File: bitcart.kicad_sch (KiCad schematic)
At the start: 8 parts

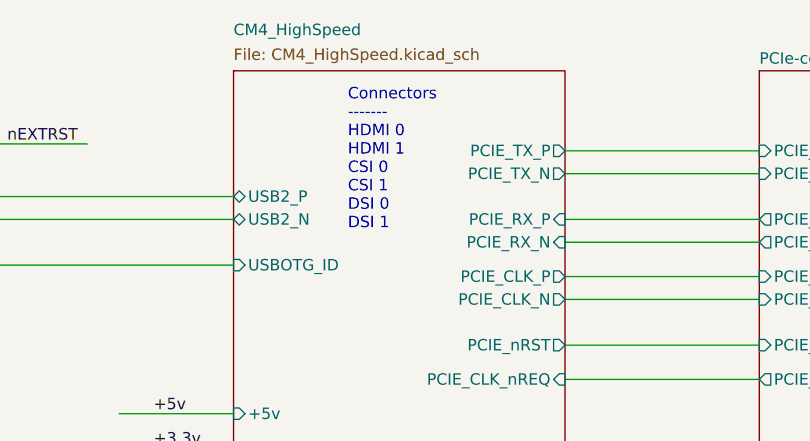
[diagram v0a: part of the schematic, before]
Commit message: removed HDMI, CAM and DISP1 connectors
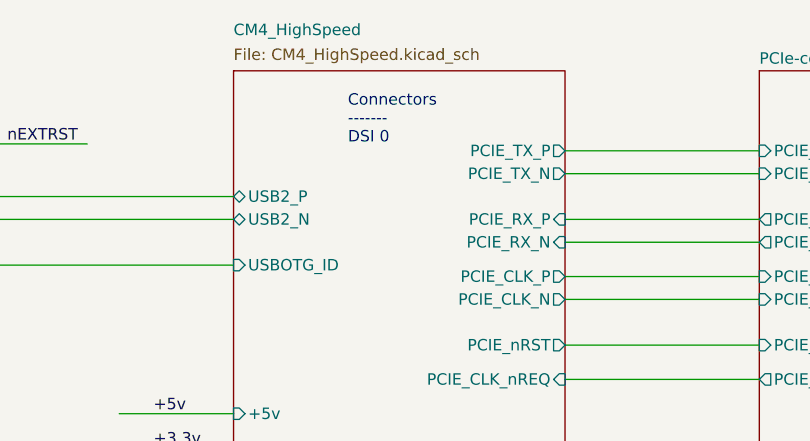
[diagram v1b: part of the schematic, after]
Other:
- note added: "Connectors ------- DSI 0"
- note removed: "Connectors ------- HDMI 0 HDMI 1 CSI 0 CSI 1 DSI 0 DSI 1"
- company: © 2020-2022 Raspberry Pi Ltd (formerly Raspberry Pi (Trading) Ltd.) -> (none)
- title: Compute Module 4 IO Board - Top Level -> Bitcart
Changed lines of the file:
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@@
   (paper "A4")
   (title_block
-    (title "Compute Module 4 IO Board - Top Level")
+    (title "Bitcart")
+    (date "2023-09-15")
     (rev "1")
-    (company "© 2020-2022 Raspberry Pi Ltd (formerly Raspberry Pi (Trading) Ltd.)")
-    (comment 1 "www.raspberrypi.com")
   )
   (junction (at 140.97 110.49) (diameter 1.016) (color 0 0 0 0)
@@
     (effects (font (size 1.27 1.27)) (justify left bottom))
   )
-  (text "Connectors\n-------\nHDMI 0\nHDMI 1\nCSI 0\nCSI 1\nDSI 0\nDSI 1"
-    (at 144.78 57.15 0)
+  (text "Connectors\n-------\nDSI 0" (at 144.78 47.625 0)
     (effects (font (size 1.27 1.27)) (justify left bottom))
   )
@@
   (sheet (at 81.28 39.878) (size 24.13 28.702)
     (stroke (width 0.1524) (type solid) (color 132 0 132 1))
-    (fill (color 255 255 255 0.0000))
+    (fill (color 255 255 194 1.0000))
     (property "Sheetname" "USB2-HUB" (at 81.28 39.2425 0)
       (effects (font (size 1.27 1.27)) (justify left bottom))

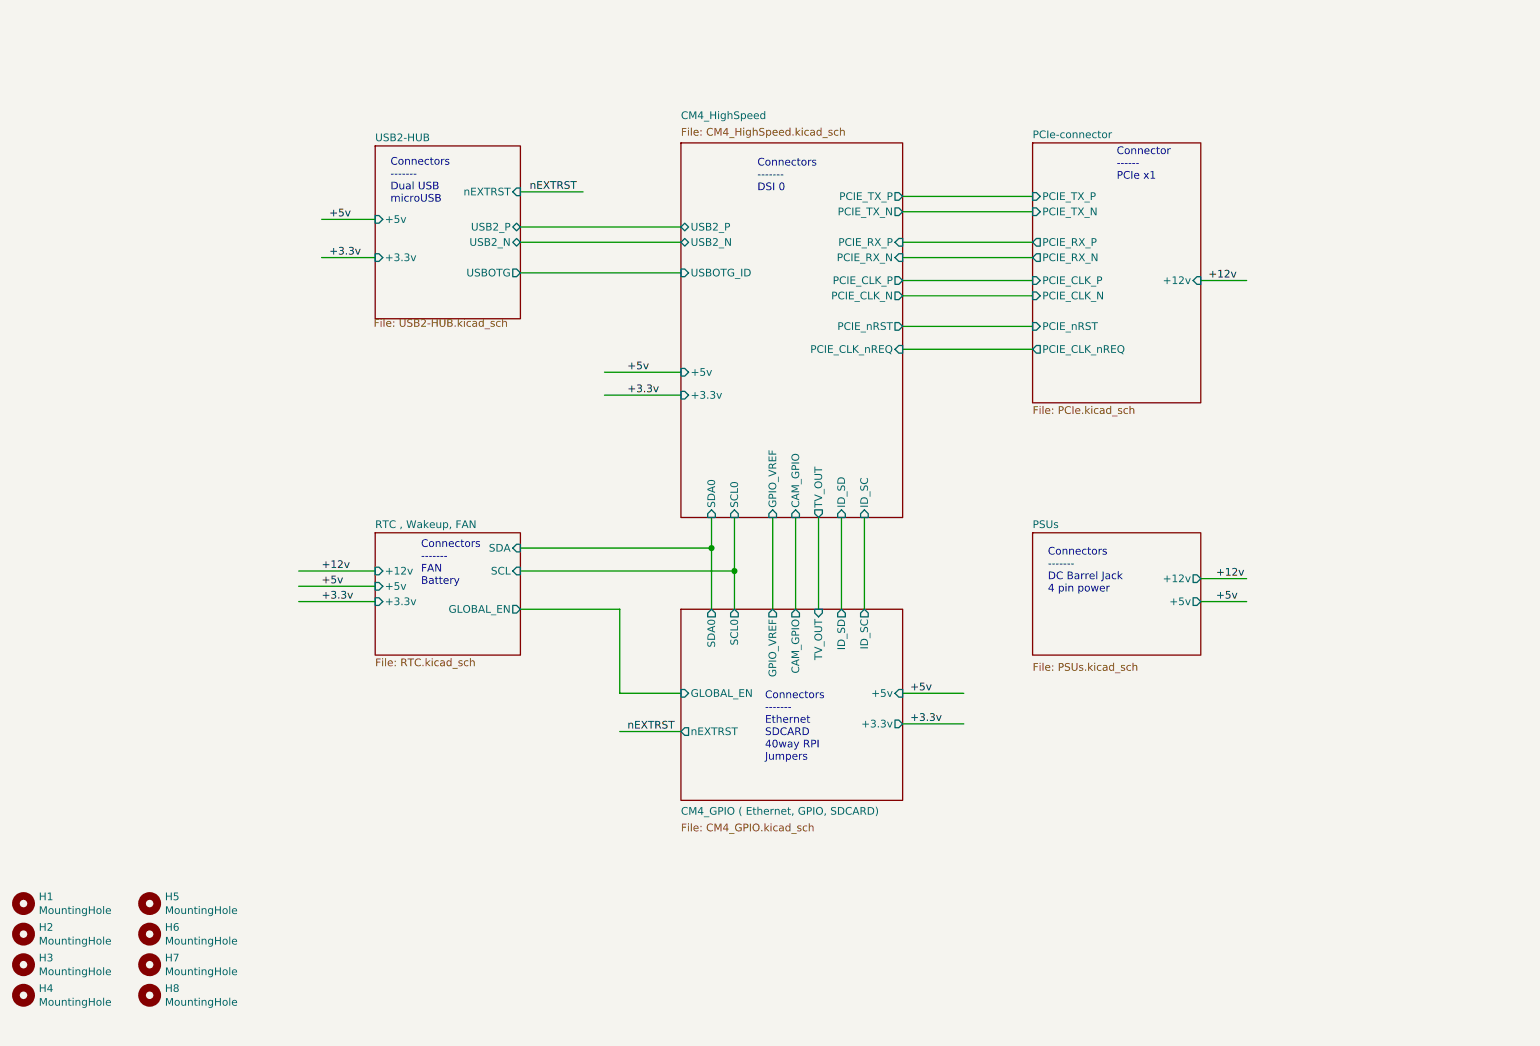
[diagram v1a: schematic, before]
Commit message: added hashboard connectors. added GPU power connector
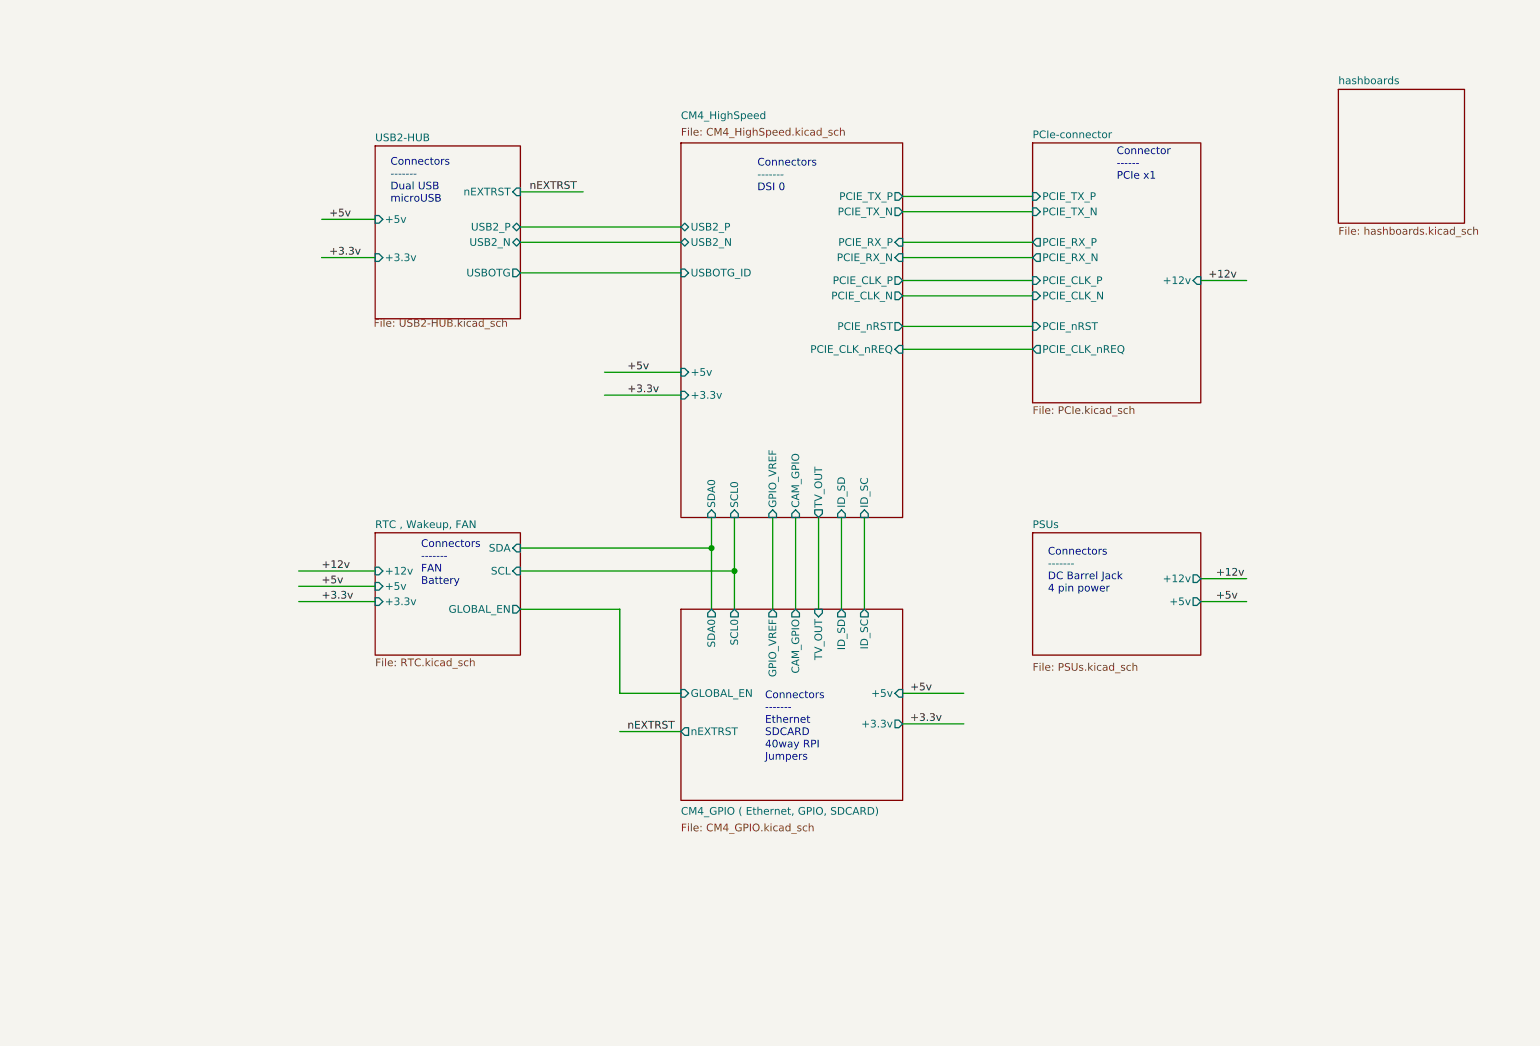
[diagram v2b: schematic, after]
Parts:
- removed H1, H2, H3, H4, H5, H6, H7, H8: MountingHole, MountingHole:MountingHole_2.7mm_M2.5, symbol Mechanical:MountingHole
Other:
- added sheet hashboards (hashboards.kicad_sch)

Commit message: extended the board to make room for IO connectors. added the vertical display connector.
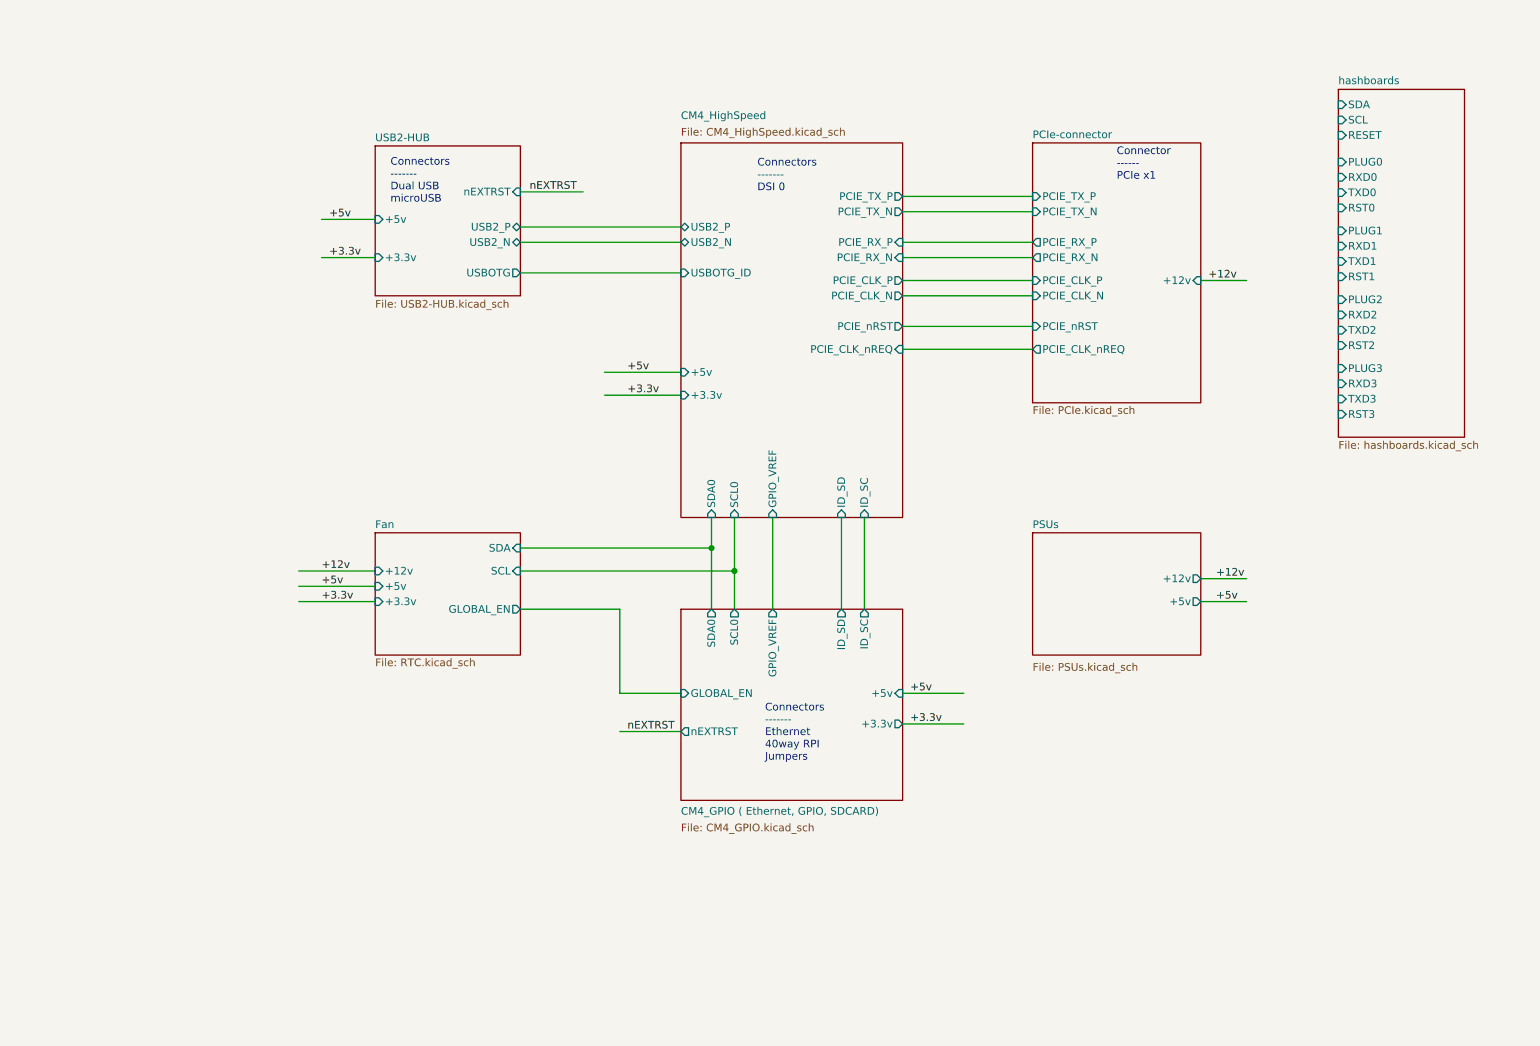
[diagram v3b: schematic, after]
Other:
- sheet RTC , Wakeup, FAN renamed Fan
- sheet CM4_GPIO ( Ethernet, GPIO, SDCARD) ports: added none; removed CAM_GPIO, TV_OUT
- sheet CM4_HighSpeed ports: added none; removed CAM_GPIO, TV_OUT
- sheet hashboards ports: added PLUG0, PLUG1, PLUG2, PLUG3, RESET, RST0, RST1, RST2, RST3, RXD0, RXD1, RXD2, RXD3, SCL, SDA, TXD0, TXD1, TXD2, TXD3; removed none
- note added: "Connectors ------- Ethernet 40way RPI Jumpers"
- note removed: "Connectors ------- DC Barrel Jack 4 pin power"
- note removed: "Connectors ------- Ethernet SDCARD 40way RPI Jumpers"
- note removed: "Connectors ------- FAN Battery"
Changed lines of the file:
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@@
-    (stroke (width 0) (type solid))
-  )
-  (wire (pts (xy 151.13 116.84) (xy 151.13 101.6))
     (stroke (width 0) (type solid))
   )
@@
     (stroke (width 0) (type solid))
   )
-  (wire (pts (xy 154.94 116.84) (xy 154.94 101.6))
-    (stroke (width 0) (type solid))
-  )
   (wire (pts (xy 105.41 60.96) (xy 132.08 60.96))
     (stroke (width 0) (type solid))
@@
     (stroke (width 0) (type solid))
   )
-  (text "Connectors\n-------\nFAN\nBattery" (at 88.9 113.03 0)
-    (effects (font (size 1.27 1.27)) (justify left bottom))
-  )
   (text "Connector\n------\nPCIe x1" (at 204.47 45.72 0)
     (effects (font (size 1.27 1.27)) (justify left bottom))
   )
-  (text "Connectors\n-------\nDC Barrel Jack\n4 pin power" (at 193.04 114.3 0)
-    (effects (font (size 1.27 1.27)) (justify left bottom))
-  )
   (text "Connectors\n-------\nDual USB\nmicroUSB" (at 83.82 49.53 0)
     (effects (font (size 1.27 1.27)) (justify left bottom))
   )
-  (text "Connectors\n-------\nEthernet\nSDCARD\n40way RPI\nJumpers"
-    (at 146.05 142.24 0)
+  (text "Connectors\n-------\nEthernet\n40way RPI\nJumpers" (at 146.05 142.24 0)
     (effects (font (size 1.27 1.27)) (justify left bottom))
   )
@@
       (effects (font (size 1.27 1.27)) (justify right))
     )
-    (pin "CAM_GPIO" output (at 151.13 116.84 90)
-      (effects (font (size 1.27 1.27)) (justify right))
-    )
     (pin "SCL0" output (at 140.97 116.84 90)
       (effects (font (size 1.27 1.27)) (justify right))
@@
       (effects (font (size 1.27 1.27)) (justify right))
     )
-    (pin "TV_OUT" input (at 154.94 116.84 90)
-      (effects (font (size 1.27 1.27)) (justify right))
-    )
     (instances
       (project "bitcart"
@@
       (effects (font (size 1.27 1.27)) (justify left))
     )
-    (pin "CAM_GPIO" input (at 151.13 101.6 270)
-      (effects (font (size 1.27 1.27)) (justify left))
-    )
     (pin "SCL0" input (at 140.97 101.6 270)
       (effects (font (size 1.27 1.27)) (justify left))
@@
       (effects (font (size 1.27 1.27)) (justify left))
     )
-    (pin "TV_OUT" output (at 154.94 101.6 270)
-      (effects (font (size 1.27 1.27)) (justify left))
-    )
     (instances
       (project "bitcart"
@@
     )
   )
-  (sheet (at 81.28 39.878) (size 24.13 28.702)
+  (sheet (at 81.28 39.878) (size 24.13 24.892)
     (stroke (width 0.1524) (type solid))
     (fill (color 255 255 194 1.0000))
@@
       (effects (font (size 1.27 1.27)) (justify left bottom))
     )
-    (property "Sheetfile" "USB2-HUB.kicad_sch" (at 81.026 68.58 0)
+    (property "Sheetfile" "USB2-HUB.kicad_sch" (at 81.28 65.405 0)
       (effects (font (size 1.27 1.27)) (justify left top))
     )
@@
     (stroke (width 0.1524) (type solid))
     (fill (color 255 255 194 1.0000))
-    (property "Sheetname" "RTC , Wakeup, FAN" (at 81.28 103.5045 0)
+    (property "Sheetname" "Fan" (at 81.28 103.5045 0)
       (effects (font (size 1.27 1.27)) (justify left bottom))
     )
@@
     )
   )
-  (sheet (at 241.3 30.48) (size 20.955 22.225) (fields_autoplaced)
+  (sheet (at 241.3 30.48) (size 20.955 57.785) (fields_autoplaced)
     (stroke (width 0.1524) (type solid))
     (fill (color 255 255 194 1.0000))
@@
       (effects (font (size 1.27 1.27)) (justify left bottom))
     )
-    (property "Sheetfile" "hashboards.kicad_sch" (at 241.3 53.2896 0)
-      (effects (font (size 1.27 1.27)) (justify left top))
-    )
-    (instances
+    (property "Sheetfile" "hashboards.kicad_sch" (at 241.3 88.8496 0)
+      (effects (font (size 1.27 1.27)) (justify left top))
+    )
+    (pin "TXD0" input (at 241.3 47.625 180)
+      (effects (font (size 1.27 1.27)) (justify left))
+    )
+    (pin "PLUG0" input (at 241.3 42.545 180)
+      (effects (font (size 1.27 1.27)) (justify left))
+    )
+    (pin "RST0" input (at 241.3 50.165 180)
+      (effects (font (size 1.27 1.27)) (justify left))
+    )
+    (pin "RXD1" input (at 241.3 56.515 180)
+      (effects (font (size 1.27 1.27)) (justify left))
+    )
+    (pin "RXD3" input (at 241.3 79.375 180)
+      (effects (font (size 1.27 1.27)) (justify left))
+    )
+    (pin "TXD2" input (at 241.3 70.485 180)
+      (effects (font (size 1.27 1.27)) (justify left))
+    )
+    (pin "RST2" input (at 241.3 73.025 180)
+      (effects (font (size 1.27 1.27)) (justify left))
+    )
+    (pin "PLUG2" input (at 241.3 65.405 180)
+      (effects (font (size 1.27 1.27)) (justify left))
+    )
+    (pin "RST1" input (at 241.3 61.595 180)
+      (effects (font (size 1.27 1.27)) (justify left))
+    )
+    (pin "TXD1" input (at 241.3 59.055 180)
+      (effects (font (size 1.27 1.27)) (justify left))
+    )
+    (pin "PLUG1" input (at 241.3 53.975 180)
+      (effects (font (size 1.27 1.27)) (justify left))
+    )
+    (pin "SDA" input (at 241.3 33.02 180)
+      (effects (font (size 1.27 1.27)) (justify left))
+    )
+    (pin "SCL" input (at 241.3 35.56 180)
+      (effects (font (size 1.27 1.27)) (justify left))
+    )
+    (pin "RESET" input (at 241.3 38.1 180)
+      (effects (font (size 1.27 1.27)) (justify left))
+    )
+    (pin "RXD2" input (at 241.3 67.945 180)
+      (effects (font (size 1.27 1.27)) (justify left))
+    )
+    (pin "RXD0" input (at 241.3 45.085 180)
+      (effects (font (size 1.27 1.27)) (justify left))
+    )
+    (pin "TXD3" input (at 241.3 81.915 180)
+      (effects (font (size 1.27 1.27)) (justify left))
+    )
+    (pin "RST3" input (at 241.3 84.455 180)
+      (effects (font (size 1.27 1.27)) (justify left))
+    )
+    (pin "PLUG3" input (at 241.3 76.835 180)
+      (effects (font (size 1.27 1.27)) (justify left))
+    )
+    (instances

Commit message: added the PSU control connector.
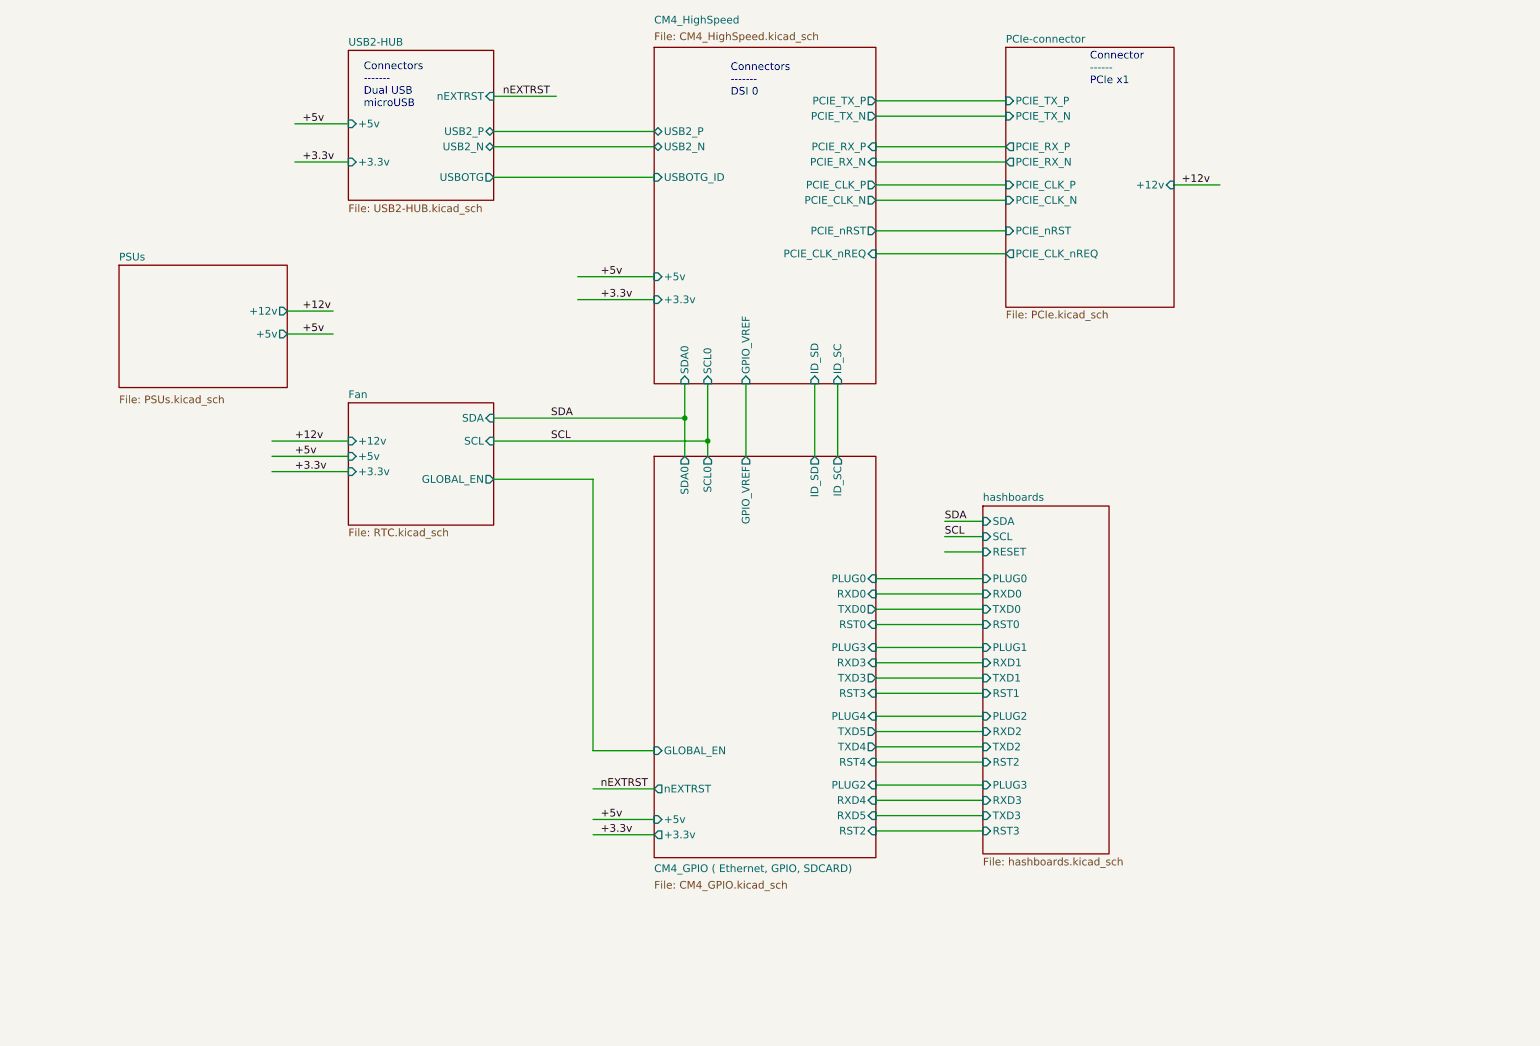
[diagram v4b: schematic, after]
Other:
- sheet CM4_GPIO ( Ethernet, GPIO, SDCARD) ports: added PLUG0, PLUG2, PLUG3, PLUG4, RST0, RST2, RST3, RST4, RXD0, RXD3, RXD4, RXD5, TXD0, TXD3, TXD4, TXD5; removed none
- note removed: "Connectors ------- Ethernet 40way RPI Jumpers"
